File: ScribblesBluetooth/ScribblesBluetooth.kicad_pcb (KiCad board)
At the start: 2 copper layers, 14 x 37.8 mm, 15 parts, among them J1 Conn_01x04, J2 Conn_01x04, J3 SWD, U1 NRF51822, Y1 32.768kHz (535-9166-2-ND)

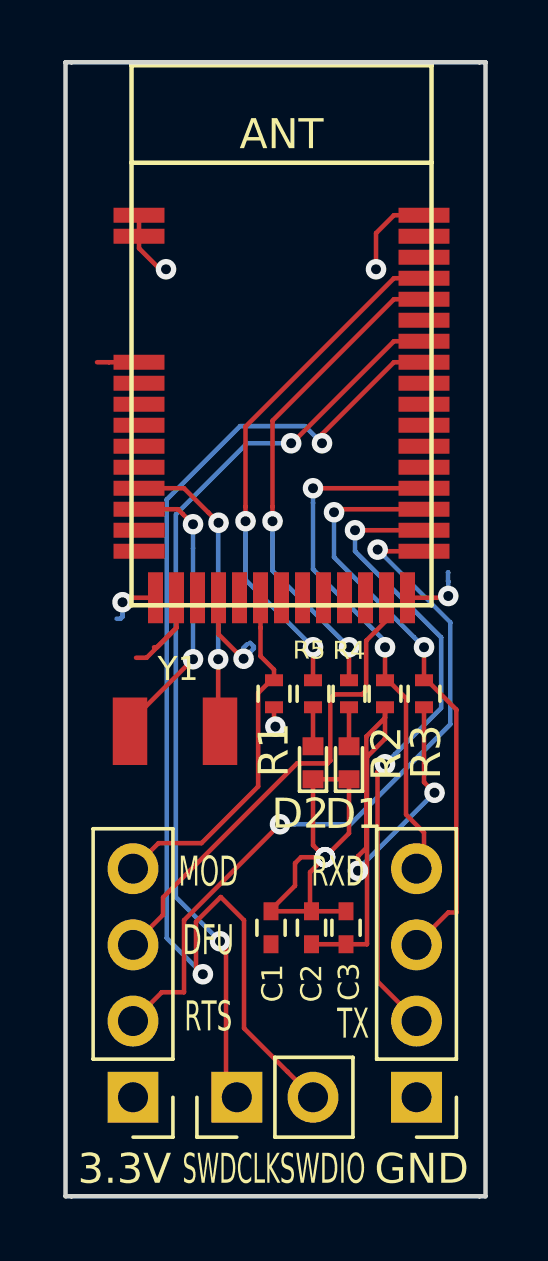
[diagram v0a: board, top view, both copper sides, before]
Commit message: Added oscillator to imu
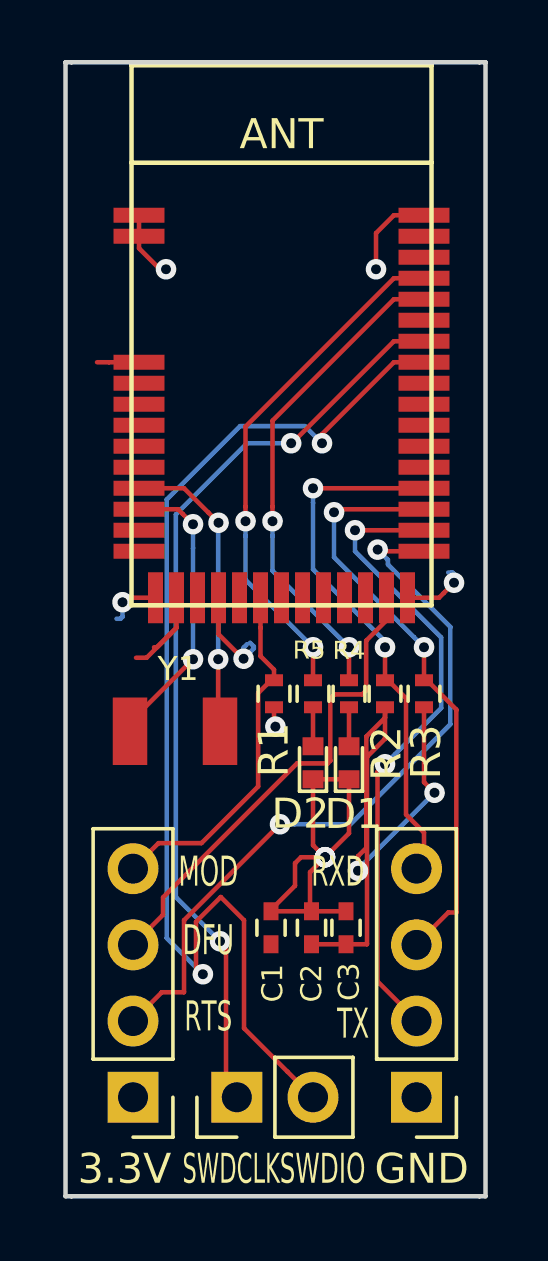
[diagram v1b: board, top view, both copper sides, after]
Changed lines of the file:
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@@
     (thickness 1.6)
     (drawings 17)
-    (tracks 217)
+    (tracks 219)
     (zones 0)
     (modules 15)
@@
   (segment (start 114.7976 93) (end 114.4 93) (width 0.1524) (layer F.Cu) (net 1))
   (segment (start 115.8 93) (end 114.7976 93) (width 0.1524) (layer F.Cu) (net 1))
+  (segment (start 125.957101 100.692899) (end 126.3 100.35) (width 0.1524) (layer F.Cu) (net 2))
+  (segment (start 125.8 100.85) (end 125.957101 100.692899) (width 0.1524) (layer F.Cu) (net 2))
+  (segment (start 124.75 100.85) (end 125.8 100.85) (width 0.1524) (layer F.Cu) (net 2))
+  (segment (start 126.108224 100.008224) (end 126.243157 100.008224) (width 0.1524) (layer B.Cu) (net 2))
+  (segment (start 126.3 100.065067) (end 126.3 100.35) (width 0.1524) (layer B.Cu) (net 2))
+  (via (at 126.3 100.35) (size 0.6858) (drill 0.3302) (layers F.Cu B.Cu) (net 2))
+  (segment (start 126.243157 100.008224) (end 126.3 100.065067) (width 0.1524) (layer B.Cu) (net 2))
   (segment (start 121.7 111.3) (end 121.5 111.1) (width 0.1524) (layer F.Cu) (net 2))
   (segment (start 121.5 111.1) (end 121.5 110) (width 0.1524) (layer F.Cu) (net 2))
@@
   (via (at 119.284799 102.882218) (size 0.6858) (drill 0.3302) (layers F.Cu B.Cu) (net 2))
   (via (at 115.25 101) (size 0.6858) (drill 0.3302) (layers F.Cu B.Cu) (net 2))
-  (segment (start 126.1 100) (end 126.108224 100.008224) (width 0.1524) (layer B.Cu) (net 2))
-  (segment (start 126.1 100.298619) (end 126.1 100) (width 0.1524) (layer B.Cu) (net 2))
-  (segment (start 126.108224 100.791776) (end 126.108224 100.306843) (width 0.1524) (layer B.Cu) (net 2))
-  (segment (start 126.108224 100.306843) (end 126.1 100.298619) (width 0.1524) (layer B.Cu) (net 2))
-  (segment (start 124.75 100.85) (end 126.05 100.85) (width 0.1524) (layer F.Cu) (net 2))
-  (segment (start 126.05 100.85) (end 126.108224 100.791776) (width 0.1524) (layer F.Cu) (net 2))
-  (via (at 126.108224 100.791776) (size 0.6858) (drill 0.3302) (layers F.Cu B.Cu) (net 2))
   (segment (start 120.3 104.5) (end 120.3 105.1) (width 0.1524) (layer F.Cu) (net 2))
   (segment (start 120.3 105.1) (end 120.345888 105.145888) (width 0.1524) (layer F.Cu) (net 2))
@@
   (segment (start 122.090083 106.371399) (end 121.067119 106.371399) (width 0.1524) (layer F.Cu) (net 5))
   (segment (start 121.067119 106.371399) (end 116.6 110.838518) (width 0.1524) (layer F.Cu) (net 5))
+  (segment (start 124.097011 99.742835) (end 126.176313 101.822137) (width 0.1524) (layer B.Cu) (net 6))
+  (segment (start 126.176313 105.069511) (end 122.845824 108.4) (width 0.1524) (layer B.Cu) (net 6))
+  (segment (start 123.754112 99.245888) (end 124.097011 99.588787) (width 0.1524) (layer B.Cu) (net 6))
+  (segment (start 124.097011 99.588787) (end 124.097011 99.742835) (width 0.1524) (layer B.Cu) (net 6))
+  (segment (start 126.176313 101.822137) (end 126.176313 105.069511) (width 0.1524) (layer B.Cu) (net 6))
+  (segment (start 122.845824 108.4) (end 120.984933 108.4) (width 0.1524) (layer B.Cu) (net 6))
+  (segment (start 120.984933 108.4) (end 120.5 108.4) (width 0.1524) (layer B.Cu) (net 6))
   (segment (start 117.3 114) (end 116.56 114) (width 0.1524) (layer F.Cu) (net 6))
   (segment (start 116.56 114) (end 115.6 114.96) (width 0.1524) (layer F.Cu) (net 6))
   (segment (start 120.5 108.4) (end 117.3 111.6) (width 0.1524) (layer F.Cu) (net 6))
   (segment (start 117.3 111.6) (end 117.3 114) (width 0.1524) (layer F.Cu) (net 6))
-  (segment (start 126.176313 101.668089) (end 126.176313 105.069511) (width 0.1524) (layer B.Cu) (net 6))
-  (segment (start 123.754112 99.245888) (end 126.176313 101.668089) (width 0.1524) (layer B.Cu) (net 6))
-  (segment (start 122.845824 108.4) (end 120.984933 108.4) (width 0.1524) (layer B.Cu) (net 6))
-  (segment (start 126.176313 105.069511) (end 122.845824 108.4) (width 0.1524) (layer B.Cu) (net 6))
-  (segment (start 120.984933 108.4) (end 120.5 108.4) (width 0.1524) (layer B.Cu) (net 6))
   (via (at 120.5 108.4) (size 0.6858) (drill 0.3302) (layers F.Cu B.Cu) (net 6))
   (segment (start 125.3 99.3) (end 123.808224 99.3) (width 0.1524) (layer F.Cu) (net 6))
